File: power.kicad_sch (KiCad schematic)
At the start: 137 parts, among them J3 Conn_01x01, J4 Conn_01x01, U1 CSD95472Q5MC, U16 CSD95472Q5MC, U3 TPS53647, U36 MCP1824T-1202E, U4 CSD95472Q5MC, U5 CSD95472Q5MC, U6 AP3211, U7 MCP1824T-0802E

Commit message: Kicad9
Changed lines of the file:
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@@
 (kicad_sch
-	(version 20231120)
+	(version 20250114)
 	(generator "eeschema")
-	(generator_version "8.0")
+	(generator_version "9.0")
 	(paper "A3")
 	(title_block
@@
 		(rev "202")
 	)
+	(text "default\nOff"
+		(exclude_from_sim no)
+		(at 125.73 262.89 0)
+		(effects
+			(font
+				(size 1.27 1.27)
+			)
+		)
+	)
+	(text "for IMAX=180A"
+		(exclude_from_sim no)
+		(at 36.83 120.65 90)
+		(effects
+			(font
+				(size 1.27 1.27)
+			)
+		)
+	)
+	(text "100k = NVM"
+		(exclude_from_sim no)
+		(at 43.18 92.71 90)
+		(effects
+			(font
+				(size 1.27 1.27)
+			)
+		)
+	)
 	(junction
 		(at 285.75 120.65)
@@
 		)
 	)
-	(text "default\nOff"
-		(exclude_from_sim no)
-		(at 125.73 262.89 0)
-		(effects
-			(font
-				(size 1.27 1.27)
-			)
-		)
-	)
-	(text "for IMAX=180A"
-		(exclude_from_sim no)
-		(at 36.83 120.65 90)
-		(effects
-			(font
-				(size 1.27 1.27)
-			)
-		)
-	)
-	(text "100k = NVM"
-		(exclude_from_sim no)
-		(at 43.18 92.71 90)
-		(effects
-			(font
-				(size 1.27 1.27)
-			)
-		)
-	)
 	(label "TPS_TSEN"
 		(at 231.14 195.58 0)
-		(fields_autoplaced yes)
 		(effects
 			(font
@@
 	(label "TPS_PWM1"
 		(at 87.63 96.52 90)
-		(fields_autoplaced yes)
 		(effects
 			(font
@@
 	(label "FCCM"
 		(at 181.61 191.77 180)
-		(fields_autoplaced yes)
 		(effects
 			(font
@@
 	(label "TPS_CSP1"
 		(at 57.15 115.57 180)
-		(fields_autoplaced yes)
 		(effects
 			(font
@@
 	(label "FCCM"
 		(at 181.61 142.24 180)
-		(fields_autoplaced yes)
 		(effects
 			(font
@@
 	(label "TPS_PWM4"
 		(at 95.25 86.36 270)
-		(fields_autoplaced yes)
 		(effects
 			(font
@@
 	(label "{slash}RESET"
 		(at 125.73 133.35 0)
-		(fields_autoplaced yes)
 		(effects
 			(font
@@
 	(label "TPS_CSP4"
 		(at 182.88 204.47 180)
-		(fields_autoplaced yes)
 		(effects
 			(font
@@
 	(label "TPS_TSEN"
 		(at 82.55 96.52 90)
-		(fields_autoplaced yes)
 		(effects
 			(font
@@
 	(label "TPS_PWM3"
 		(at 92.71 86.36 270)
-		(fields_autoplaced yes)
 		(effects
 			(font
@@
 	(label "TPS_CSP4"
 		(at 57.15 123.19 180)
-		(fields_autoplaced yes)
 		(effects
 			(font
@@
 	(label "TPS_TSEN"
 		(at 231.14 102.87 0)
-		(fields_autoplaced yes)
 		(effects
 			(font
@@
 	(label "TPS_PWM1"
 		(at 193.04 96.52 180)
-		(fields_autoplaced yes)
 		(effects
 			(font
@@
 	(label "FCCM"
 		(at 181.61 99.06 180)
-		(fields_autoplaced yes)
 		(effects
 			(font
@@
 	(label "TPS_PWM2"
 		(at 193.04 139.7 180)
-		(fields_autoplaced yes)
 		(effects
 			(font
@@
 	(label "TPS_TSEN"
 		(at 229.87 52.07 0)
-		(fields_autoplaced yes)
 		(effects
 			(font
@@
 	(label "TPS_CSP2"
 		(at 57.15 118.11 180)
-		(fields_autoplaced yes)
 		(effects
 			(font
@@
 	(label "TPS_PWM2"
 		(at 90.17 96.52 90)
-		(fields_autoplaced yes)
 		(effects
 			(font
@@
 	(label "VSENSE+"
 		(at 34.29 144.78 180)
-		(fields_autoplaced yes)
 		(effects
 			(font
@@
 	(label "TPS_PWM4"
 		(at 193.04 189.23 180)
-		(fields_autoplaced yes)
 		(effects
 			(font
@@
 	(label "TPS_CSP3"
 		(at 57.15 120.65 180)
-		(fields_autoplaced yes)
 		(effects
 			(font
@@
 	(label "VSENSE-"
 		(at 424.18 143.51 0)
-		(fields_autoplaced yes)
 		(effects
 			(font
@@
 	(label "VSENSE-"
 		(at 34.29 149.86 180)
-		(fields_autoplaced yes)
 		(effects
 			(font
@@
 	(label "TPS_CSP2"
 		(at 182.88 154.94 180)
-		(fields_autoplaced yes)
 		(effects
 			(font
@@
 	(label "TPS_CSP3"
 		(at 181.61 60.96 180)
-		(fields_autoplaced yes)
 		(effects
 			(font
@@
 	(label "TPS_CSP1"
 		(at 182.88 111.76 180)
-		(fields_autoplaced yes)
 		(effects
 			(font
@@
 	(label "FCCM"
 		(at 180.34 48.26 180)
-		(fields_autoplaced yes)
 		(effects
 			(font
@@
 	(label "VSENSE+"
 		(at 424.18 139.7 0)
-		(fields_autoplaced yes)
 		(effects
 			(font
@@
 	(label "TPS_TSEN"
 		(at 231.14 146.05 0)
-		(fields_autoplaced yes)
 		(effects
 			(font
@@
 	(label "FCCM"
 		(at 85.09 95.885 90)
-		(fields_autoplaced yes)
 		(effects
 			(font
@@
 	(label "TPS_PWM3"
 		(at 191.77 45.72 180)
-		(fields_autoplaced yes)
 		(effects
 			(font
@@
 		(shape output)
 		(at 120.65 158.75 0)
-		(fields_autoplaced yes)
 		(effects
 			(font
@@
 		(shape output)
 		(at 31.75 26.67 180)
-		(fields_autoplaced yes)
 		(effects
 			(font
@@
 		(shape input)
 		(at 31.75 29.21 180)
-		(fields_autoplaced yes)
 		(effects
 			(font
@@
 		(shape input)
 		(at 121.92 125.73 0)
-		(fields_autoplaced yes)
 		(effects
 			(font
@@
 		(shape bidirectional)
 		(at 121.92 120.65 0)
-		(fields_autoplaced yes)
 		(effects
 			(font
@@
 		(shape output)
 		(at 31.75 34.29 180)
-		(fields_autoplaced yes)
 		(effects
 			(font
@@
 		(shape output)
 		(at 31.75 31.75 180)
-		(fields_autoplaced yes)
 		(effects
 			(font
@@
 		(shape output)
 		(at 31.75 39.37 180)
-		(fields_autoplaced yes)
 		(effects
 			(font
@@
 		(shape output)
 		(at 31.75 36.83 180)
-		(fields_autoplaced yes)
 		(effects
 			(font
@@
 		(shape input)
 		(at 153.67 128.27 0)
-		(fields_autoplaced yes)
 		(effects
 			(font
@@
 		(shape input)
 		(at 128.905 243.205 180)
-		(fields_autoplaced yes)
 		(effects
 			(font
@@
 		)
 	)
+	(embedded_fonts no)
 )

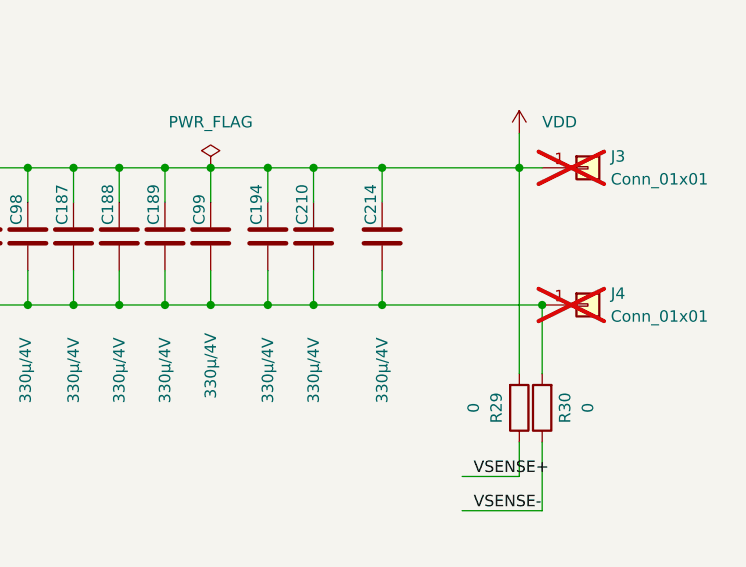
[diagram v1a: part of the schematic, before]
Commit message: Buck rotation test
Different Buck Layout
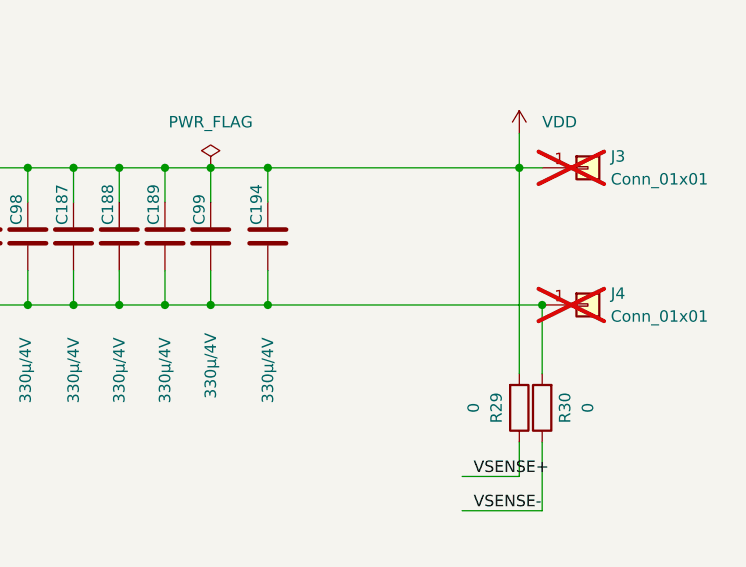
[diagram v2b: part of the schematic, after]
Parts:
- removed C210, C214: 330µ/4V, Capacitor_SMD:C_1210_3225Metric, symbol Device:C
- L1, L2, L4, L5: footprint myfootprints:IFLR-4031GC-01-8x10 -> Nerd8:IFLR-4031GC-01-8x10
- U1, U16, U4, U5: footprint myfootprints:CSD95472-SON-5x6 -> Nerd8:CSD95472-SON-5x6

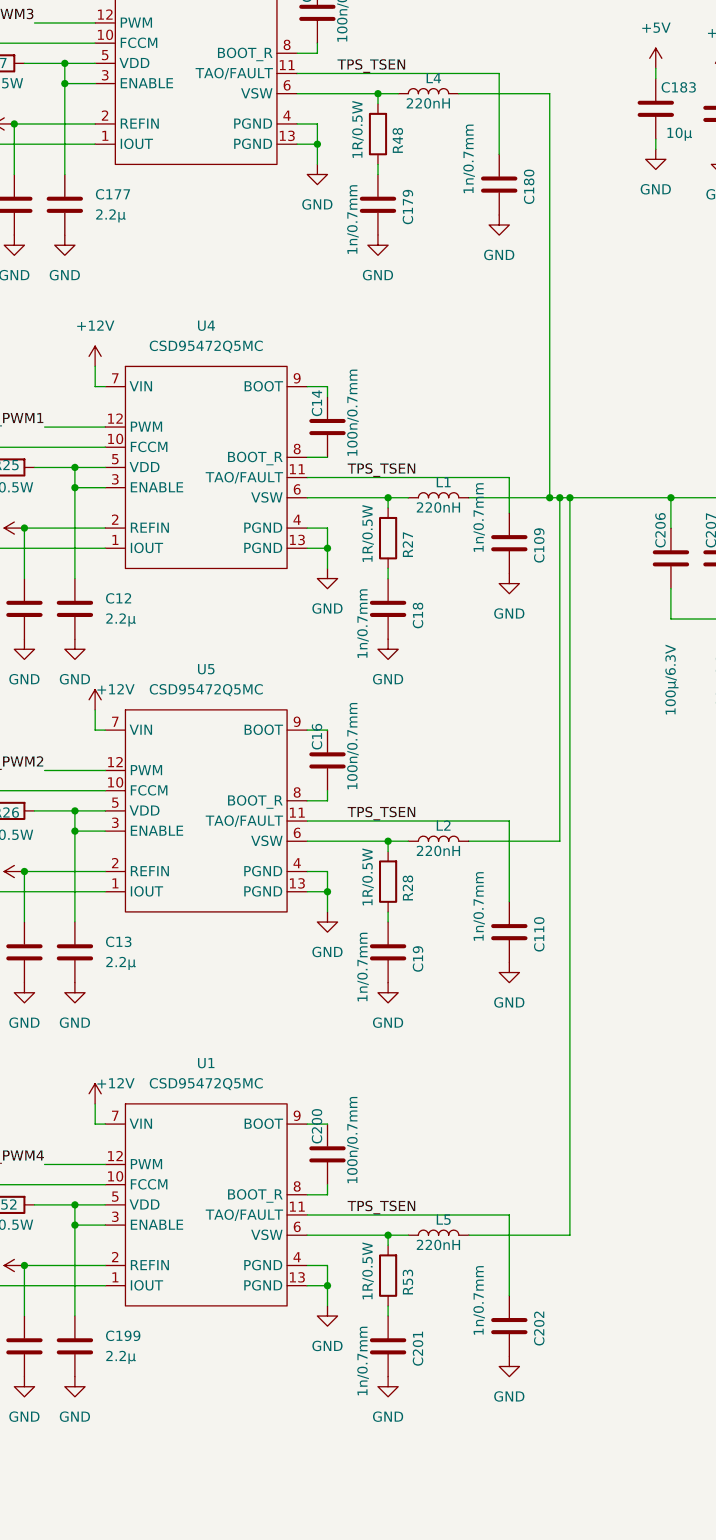
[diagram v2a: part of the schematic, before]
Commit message: Changed snubber C to 2.7nF
Changed snubber values to decrease ringing amplitude. BOM changes
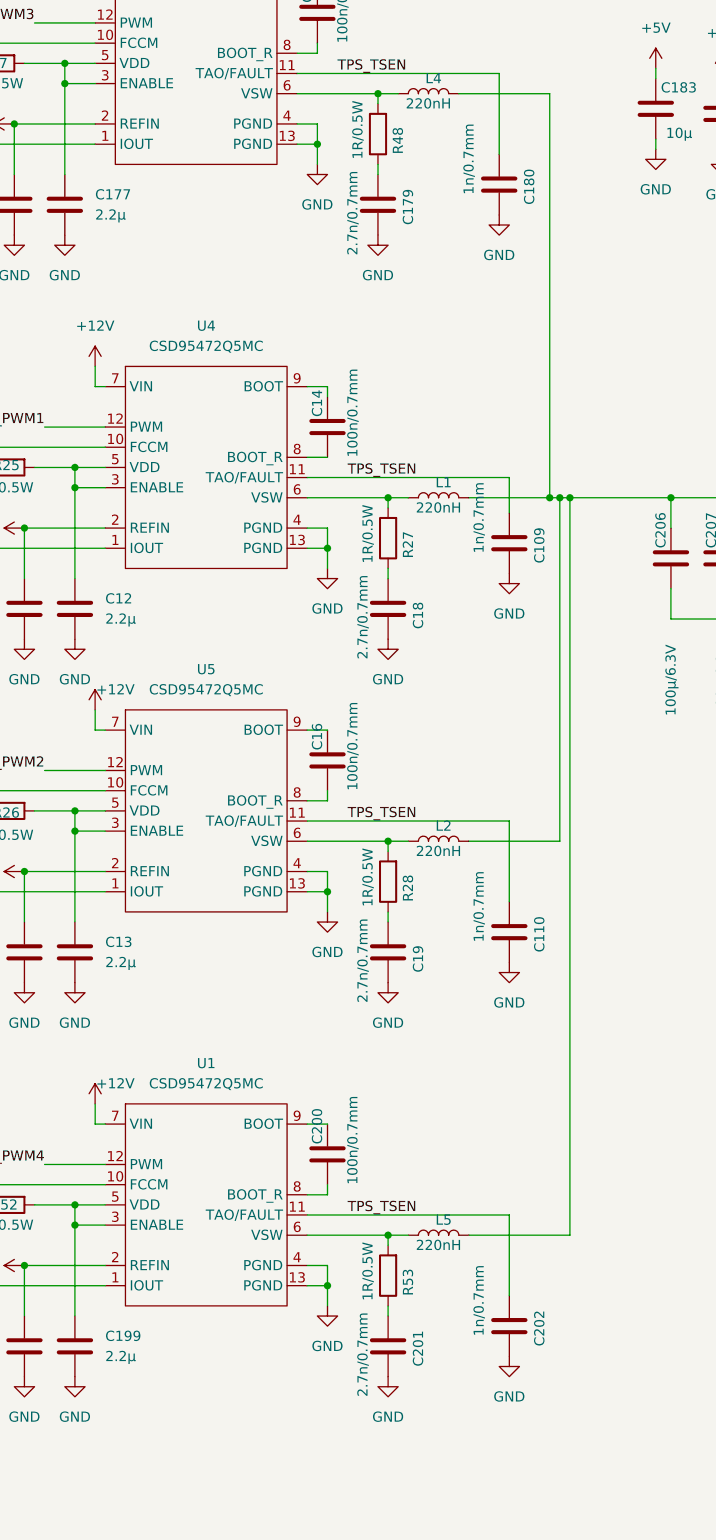
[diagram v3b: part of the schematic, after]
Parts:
- C179, C18, C19, C201: value 1n/0.7mm -> 2.7n/0.7mm; Manufacturer CC0805KRX7R0BB102 -> GRM2165C1H272JA01D; OrderNr 311-1472-1-ND -> 490-1630-1-ND
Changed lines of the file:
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@@
 			)
 		)
-		(property "Value" "1n/0.7mm"
+		(property "Value" "2.7n/0.7mm"
 			(at 231.775 74.93 90)
 			(effects
@@
 			)
 		)
-		(property "Description" "CAP CER 1000PF 100V X7R 0805"
+		(property "Description" "CAP CER 2700PF 50V C0G/NP0 0805"
 			(at 234.95 68.58 0)
 			(effects
@@
 			)
 		)
-		(property "Manufacturer" "CC0805KRX7R0BB102"
+		(property "Manufacturer" "GRM2165C1H272JA01D"
 			(at 234.95 68.58 0)
 			(effects
@@
 			)
 		)
-		(property "OrderNr" "311-1472-1-ND"
+		(property "OrderNr" "490-1630-1-ND"
 			(at 234.95 68.58 0)
 			(effects
@@
 			)
 		)
-		(property "Value" "1n/0.7mm"
+		(property "Value" "2.7n/0.7mm"
 			(at 233.045 125.73 90)
 			(effects
@@
 			)
 		)
-		(property "Description" "CAP CER 1000PF 100V X7R 0805"
+		(property "Description" "CAP CER 2700PF 50V C0G/NP0 0805"
 			(at 236.22 119.38 0)
 			(effects
@@
 			)
 		)
-		(property "Manufacturer" "CC0805KRX7R0BB102"
+		(property "Manufacturer" "GRM2165C1H272JA01D"
 			(at 236.22 119.38 0)
 			(effects
@@
 			)
 		)
-		(property "OrderNr" "311-1472-1-ND"
+		(property "OrderNr" "490-1630-1-ND"
 			(at 236.22 119.38 0)
 			(effects
@@
 			)
 		)
-		(property "Value" "1n/0.7mm"
+		(property "Value" "2.7n/0.7mm"
 			(at 233.045 168.91 90)
 			(effects
@@
 			)
 		)
-		(property "Description" "CAP CER 1000PF 100V X7R 0805"
+		(property "Description" "CAP CER 2700PF 50V C0G/NP0 0805"
 			(at 236.22 162.56 0)
 			(effects
@@
 			)
 		)
-		(property "Manufacturer" "CC0805KRX7R0BB102"
+		(property "Manufacturer" "GRM2165C1H272JA01D"
 			(at 236.22 162.56 0)
 			(effects
@@
 			)
 		)
-		(property "OrderNr" "311-1472-1-ND"
+		(property "OrderNr" "490-1630-1-ND"
 			(at 236.22 162.56 0)
 			(effects
@@
 			)
 		)
-		(property "Value" "1n/0.7mm"
+		(property "Value" "2.7n/0.7mm"
 			(at 233.045 218.44 90)
 			(effects
@@
 			)
 		)
-		(property "Description" "CAP CER 1000PF 100V X7R 0805"
+		(property "Description" "CAP CER 2700PF 50V C0G/NP0 0805"
 			(at 236.22 212.09 0)
 			(effects
@@
 			)
 		)
-		(property "Manufacturer" "CC0805KRX7R0BB102"
+		(property "Manufacturer" "GRM2165C1H272JA01D"
 			(at 236.22 212.09 0)
 			(effects
@@
 			)
 		)
-		(property "OrderNr" "311-1472-1-ND"
+		(property "OrderNr" "490-1630-1-ND"
 			(at 236.22 212.09 0)
 			(effects
